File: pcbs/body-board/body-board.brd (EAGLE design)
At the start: 65 x 44.5 mm, 27 parts, among them X1 2520-

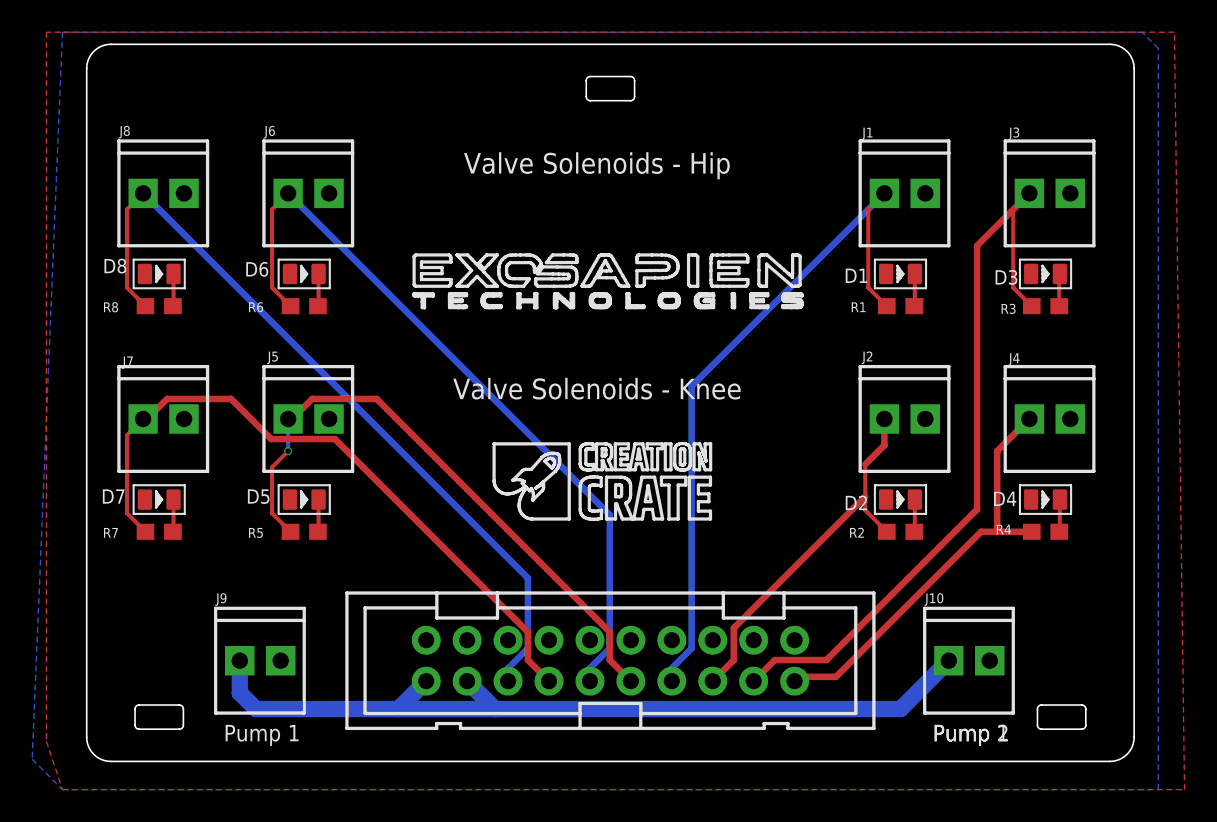
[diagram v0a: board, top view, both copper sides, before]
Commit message: change zip tie position
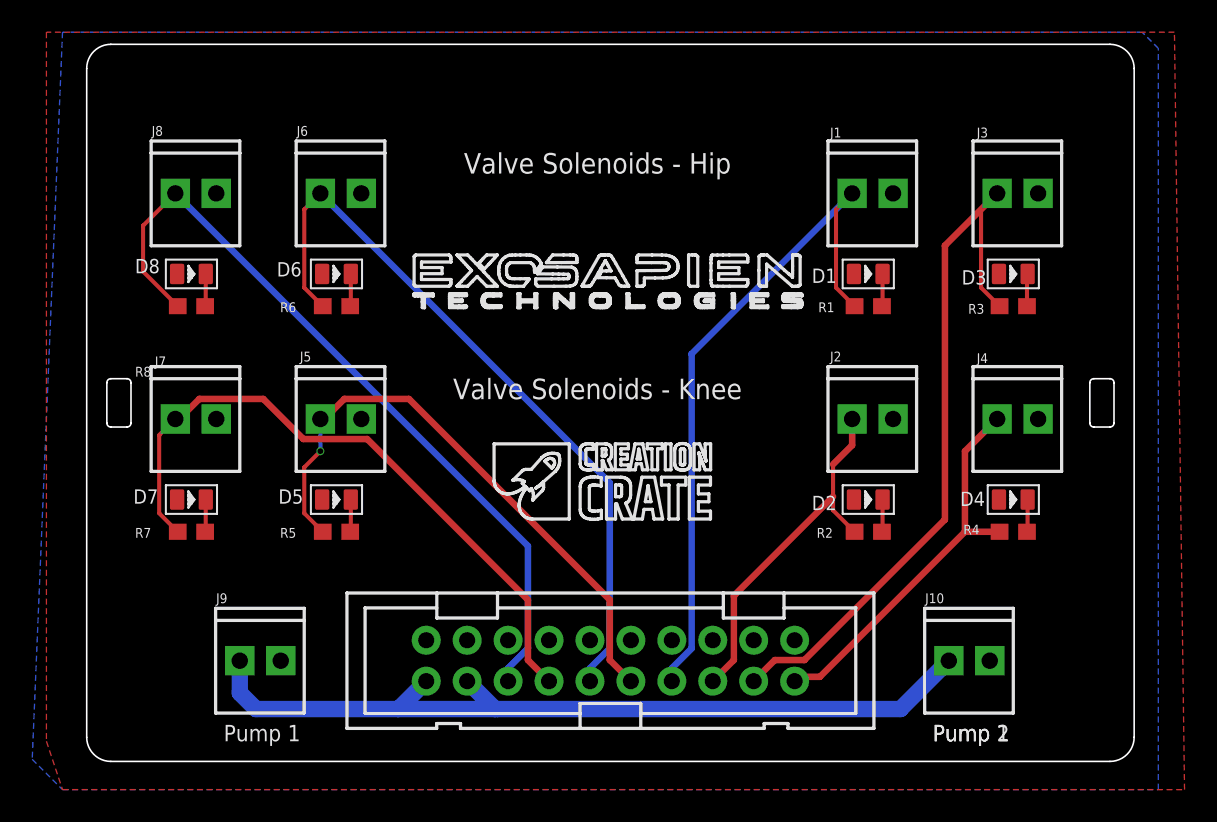
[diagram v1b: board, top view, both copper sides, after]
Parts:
- moved D1 2.00 mm to (49.0, 30.0)
- moved D2 2.00 mm to (49.0, 16.0)
- moved D3 2.00 mm to (58.0, 30.0)
- moved D4 2.00 mm to (58.0, 16.0)
- moved D5 2.00 mm to (16.0, 16.0)
- moved D6 2.00 mm to (16.0, 30.0)
- moved D7 2.00 mm to (7.00, 16.0)
- moved D8 2.00 mm to (7.00, 30.0)
- moved J1 2.00 mm to (48.0, 35.0)
- moved J2 2.00 mm to (48.0, 21.0)
- moved J3 2.00 mm to (57.0, 35.0)
- moved J4 2.00 mm to (57.0, 21.0)
- moved J5 2.00 mm to (15.0, 21.0)
- moved J6 2.00 mm to (15.0, 35.0)
- moved J7 2.00 mm to (6.00, 21.0)
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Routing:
- net N$16: track 26.4 -> 24.4 mm
- net N$15: track 47.1 -> 45.5 mm
- net N$14: track 23.4 -> 22.6 mm
- net N$11: track 46.9 -> 46.1 mm
- net N$10: track 41.9 -> 41.0 mm
- net N$13: track 43.6 -> 42.8 mm
- net N$12: track 38.0 -> 37.1 mm
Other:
- outline, holes or cut-outs redrawn
